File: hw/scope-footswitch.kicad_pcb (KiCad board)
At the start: 2 copper layers, 80 x 50 mm, 31 parts, among them J1 CN00050, J2 CN00023, J3 CN00049, SW1 M00027, SW2 M00012, SW3 M00026, Y1 Y00015

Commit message: Initial completion of schematic and layout
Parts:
- added C10: C00004, footprints:C_0805_2012M, F.Cu at (165.1, 82.5)
- added C11: C00033, footprints:C_0402_1005M, F.Cu at (143.8, 96.7)
- added C12: C00007, footprints:C_0603_1608M, F.Cu at (158.4, 100.5)
- added C13: C00001, footprints:C_0402_1005M, F.Cu at (158.6, 99.2)
- added C14: C00001, footprints:C_0402_1005M, F.Cu at (154.1, 89.0)
- added C15: C00001, footprints:C_0402_1005M, F.Cu at (151.6, 90.0)
- added C16: C00001, footprints:C_0402_1005M, F.Cu at (162.3, 90.7)
- added C17: C00001, footprints:C_0402_1005M, F.Cu at (160.4, 99.8)
- added C18: C00001, footprints:C_0402_1005M, F.Cu at (150.6, 95.2)
- added C19: C00001, footprints:C_0402_1005M, F.Cu at (128.6, 104.5)
- added C20: C00002, footprints:C_0603_1608M, F.Cu at (163.6, 90.5)
- added C21: C00001, footprints:C_0402_1005M, F.Cu at (128.6, 99.0)
- added C22: C00001, footprints:C_0402_1005M, F.Cu at (114.8, 86.5)
- added C23: C00001, footprints:C_0402_1005M, F.Cu at (165.6, 88.7)
- added C24: C00003, footprints:CRADIAL_6.3x11.2_2.5, F.Cu at (169.6, 106.7)
- added C25: C00027, footprints:C_0402_1005M, F.Cu at (182.2, 85.0)
- added C26: C00027, footprints:C_0402_1005M, F.Cu at (172.8, 112.8)
- added C27: C00001, footprints:C_0402_1005M, F.Cu at (168.2, 100.5)
- added C28: C00002, footprints:C_0603_1608M, F.Cu at (183.3, 95.0)
- added C29: C00001, footprints:C_0402_1005M, F.Cu at (179.4, 86.2)
- added D1: D00005, footprints:SOT_3_950_2900X1300X1000_ONSEMI, F.Cu at (175.6, 85.2)
- added P1: CN00052, footprints:P_FCI_68000-206, F.Cu at (148.4, 109.2)
- added P2: CN00051, footprints:P_CNC_3221-10-0300-00, F.Cu at (153.8, 79.7)
- added Q1: Q00002, footprints:SOT_6_650_2150X1300x1100_DIODES, F.Cu at (119.6, 86.5)
- added R12: R00038, footprints:R_0402_1005M, F.Cu at (134.8, 85.5)
- added R13: R00014, footprints:R_0402_1005M, F.Cu at (176.6, 92.2)
- added R14: R00009, footprints:R_0402_1005M, F.Cu at (176.6, 93.2)
- added R15: R00014, footprints:R_0402_1005M, F.Cu at (134.8, 97.0)
- added R16: R00014, footprints:R_0402_1005M, F.Cu at (133.6, 97.0)
- added R17: R00014, footprints:R_0402_1005M, F.Cu at (132.3, 97.0)
- added R18: R00014, footprints:R_0402_1005M, F.Cu at (148.8, 89.5)
- added R19: R00011, footprints:R_0402_1005M, F.Cu at (120.1, 102.7)
- added R20: R00011, footprints:R_0402_1005M, F.Cu at (120.1, 100.7)
- added R21: R00014, footprints:R_0402_1005M, F.Cu at (158.6, 101.8)
- added R22: R00014, footprints:R_0402_1005M, F.Cu at (127.1, 104.5)
- added R23: R00014, footprints:R_0402_1005M, F.Cu at (127.1, 99.0)
- added R24: R00014, footprints:R_0402_1005M, F.Cu at (127.8, 102.7)
- added R25: R00014, footprints:R_0402_1005M, F.Cu at (127.8, 100.7)
- added R26: R00014, footprints:R_0402_1005M, F.Cu at (114.1, 88.5)
- added R27: R00014, footprints:R_0402_1005M, F.Cu at (124.1, 87.0)
- added R28: R00014, footprints:R_0402_1005M, F.Cu at (113.3, 86.5)
- added R29: R00079, footprints:R_0603_1608M, F.Cu at (120.8, 89.0)
- added R30: R00014, footprints:R_0402_1005M, F.Cu at (122.6, 87.0)
- added R31: R00079, footprints:R_0603_1608M, F.Cu at (117.6, 89.0)
- added R32: R00014, footprints:R_0402_1005M, F.Cu at (163.1, 102.7)
- added R33: R00014, footprints:R_0402_1005M, F.Cu at (161.6, 99.8)
- added R34: R00047, footprints:R_0402_1005M, F.Cu at (170.6, 88.7)
- added R35: R00016, footprints:R_0402_1005M, F.Cu at (163.1, 109.5)
- added R36: R00047, footprints:R_0402_1005M, F.Cu at (168.1, 88.7)
- added R37: R00047, footprints:R_0402_1005M, F.Cu at (169.3, 88.7)
- added R38: R00047, footprints:R_0402_1005M, F.Cu at (166.8, 88.7)
- added R39: R00008, footprints:R_0402_1005M, F.Cu at (182.2, 83.8)
- added R40: R00008, footprints:R_0402_1005M, F.Cu at (172.8, 111.7)
- added R41: R00014, footprints:R_0402_1005M, F.Cu at (172.8, 85.2)
- added U1: U00054, footprints:SOT_5_950_2900X1600X1100_DIODES, F.Cu at (128.8, 86.5)
- added U2: U00086, footprints:SOT_6_950_2800x1600x110_DIODES_SOT26, F.Cu at (180.1, 93.2)
- added U3: U00055, footprints:SOIC_8_1270_4900X3900X1750, F.Cu at (134.3, 91.2)
- added U4: U00087, footprints:SOT_5_950_2900X1600X1100_DIODES, F.Cu at (148.1, 87.2)
- added U5: U00049, footprints:SOT_5_950_2900X1600X1100_DIODES, F.Cu at (165.1, 79.2)
- added U6: U00084, footprints:QFN_48_500_7000X7000X600_ST, F.Cu at (156.8, 93.7)
- added U7: U00085, footprints:MSOP_10_500_3000X3000X1100_ONSEMI, F.Cu at (168.8, 92.7)
- added U8: U00086, footprints:SOT_6_950_2800x1600x110_DIODES_SOT26, F.Cu at (163.6, 106.7)
- C2, C3: value C00033 -> C00001
- C5, C8: value C00002 -> C00001; footprint footprints:C_0603_1608M -> footprints:C_0402_1005M
- C6: value C00004 -> C00002; footprint footprints:C_0805_2012M -> footprints:C_0603_1608M
- C9: value C00001 -> C00033
- J2: value CN00023 -> CN00049; footprint footprints:J_FCI_10118194 -> footprints:J_AMPHENOL_UE27AC54100
- J3: value CN00049 -> CN00023; footprint footprints:J_AMPHENOL_UE27AC54100 -> footprints:J_FCI_10118194
- R10: value R00014 -> R00038
- R11, R4: value R00016 -> R00014
- R2: value R00025 -> R00016; footprint R_0603_1608M -> footprints:R_0402_1005M
- R7: value R00014 -> R00056
- R9: value R00009 -> R00037
- moved D5 79.6 mm to (180.1, 88.7), turned to 180 degrees
- moved J2 75.1 mm to (178.1, 104.7)
- moved SW1 57.4 mm to (186.0, 78.5)
- moved J1 57.3 mm to (110.6, 108.2)
- moved SW3 57.3 mm to (111.2, 94.2)
- moved D2 57.0 mm to (124.6, 80.2)
- moved SW2 57.0 mm to (139.6, 80.2)
- moved R7 54.5 mm to (172.2, 82.7), turned to 180 degrees
- moved D4 48.1 mm to (170.8, 99.5), turned to 270 degrees
- moved R3 44.9 mm to (155.7, 84.7), turned to 180 degrees
- moved Y1 41.7 mm to (146.8, 95.2), turned to 270 degrees
- moved J3 40.8 mm to (187.2, 88.2)
- moved R6 37.9 mm to (172.2, 81.6)
- moved R4 36.9 mm to (151.1, 84.7)
- moved C6 36.4 mm to (165.3, 76.2)
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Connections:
- C2 pad 1: GND -> /BTN
- C2 pad 2: Net-(C2-Pad2) -> GND
- C3 pad 1: GND -> +5V
- C3 pad 2: Net-(C3-Pad2) -> GND
- C4 pad 1: /BTN -> +5V
- C5 pad 1: GND -> +3V3
- C5 pad 2: +5V -> GND
- C6 pad 1: +3V3 -> GND
- C6 pad 2: GND -> +5V
- C7 pad 1: /HOST_VBUS -> +3V3
- C8 pad 1: GND -> +3V3
- C8 pad 2: VBUS -> GND
- C9 pad 1: VBUS -> GND
- C9 pad 2: GND -> Net-(C9-Pad2)
- D2 pad 2: Net-(D2-Pad2) -> GND
- D2 pad 3: (no net) -> /LED_DATA
- D2 pad 4: Net-(D2-Pad4) -> +5V
- D3 pad 1: Net-(D3-Pad1) -> /FOOTSW_BTN1_R
- D3 pad 2: Net-(D3-Pad2) -> GND
- D3 pad 3: Net-(D3-Pad3) -> /FOOTSW_BTN2_R
- D3 pad 4: Net-(D3-Pad4) -> /FOOTSW_BTN2_R
- D3 pad 5: Net-(D3-Pad5) -> +3V3
- D3 pad 6: Net-(D3-Pad6) -> /FOOTSW_BTN1_R
- D4 pad 1: Net-(D4-Pad1) -> /HOST_DP
- D4 pad 3: GND -> /HOST_DM
- D4 pad 4: GND -> /HOST_DM
- D4 pad 5: VBUS -> /HOST_VBUS
- D4 pad 6: Net-(D4-Pad6) -> /HOST_DP
- D5 pad 1: Net-(D5-Pad1) -> /DEVICE_DM
- D5 pad 3: Net-(D5-Pad3) -> /DEVICE_DP
- D5 pad 4: Net-(D5-Pad4) -> /DEVICE_DP
- D5 pad 5: /HOST_VBUS -> VBUS
- D5 pad 6: Net-(D5-Pad6) -> /DEVICE_DM
- J1 pad 1: Net-(J1-Pad1) -> GND
- J2 pad 1: VBUS -> /HOST_VBUS
- J2 pad 2: Net-(D4-Pad1) -> /HOST_DM
- J2 pad 3: Net-(D4-Pad6) -> /HOST_DP
- J2 pad 4: Net-(J2-Pad4) -> GND
- J2 pad M1: Net-(J2-PadM1) -> /HOST_SHIELD
- J2 pad M2: Net-(J2-PadM1) -> /HOST_SHIELD
- J3 pad 1: /HOST_VBUS -> VBUS
- J3 pad 2: Net-(D5-Pad1) -> /DEVICE_DM
- J3 pad 3: Net-(D5-Pad6) -> /DEVICE_DP
- J3 pad 4: GND -> Net-(J3-Pad4)
- J3 pad M1: Net-(J3-PadM1) -> /DEVICE_SHIELD
- J3 pad M2: Net-(J3-PadM2) -> /DEVICE_SHIELD
- R1 pad 1: /EN_DEVICE -> +3V3
- R1 pad 2: /EN_DEVICE_5V -> /UART_RX
- R10 pad 1: +3V3 -> /I2C_SDA
- R10 pad 2: /HOST_FAULT_N -> +3V3
- R11 pad 1: /HOST_ILIM -> GND
- R11 pad 2: GND -> Net-(R11-Pad2)
- R2 pad 1: /EN_DEVICE -> +3V3
- R2 pad 2: GND -> /SWDIO
- R3 pad 1: +3V3 -> /SWDCLK
- R3 pad 2: /SWDIO -> GND
- R4 pad 1: /SWDCLK -> +3V3
- R4 pad 2: GND -> /NRST
- R5 pad 1: /NRST -> /BTN_R
- R5 pad 2: +3V3 -> GND
- R6 pad 1: /BTN_R -> /EN_DEVICE
- R6 pad 2: /BTN -> /EN_DEVICE_5V
- R7 pad 1: /BTN -> GND
- R7 pad 2: GND -> /EN_DEVICE
- R8 pad 1: VBUS -> /BTN_R
- R8 pad 2: /VIN_FAULT_N -> /BTN
- R9 pad 1: /VIN_ILIM -> /LED_DATA
- R9 pad 2: GND -> /LED_DATA_R
- SW3 pad 2: Net-(SW3-Pad2) -> +3V3
- SW3 pad 3: Net-(SW3-Pad3) -> /MODE_R
- SW3 pad 5: Net-(SW3-Pad5) -> +3V3
- Y1 pad 1: Net-(C2-Pad2) -> Net-(C9-Pad2)
- Y1 pad 2: Net-(C3-Pad2) -> Net-(C11-Pad2)
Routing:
- net +3V3: track 0.00 -> 171.1 mm, vias 0 -> 10
- net +5V: track 0.00 -> 127.2 mm, vias 0 -> 4
- net GND: track 0.00 -> 100.7 mm, vias 0 -> 61
- net /MODE_LED_R: track 0.00 -> 53.1 mm, vias 0 -> 2
- net /MODE: track 0.00 -> 47.3 mm, vias 0 -> 2
- net /MODE_LED_G: track 0.00 -> 46.7 mm, vias 0 -> 2
- net /EN_DEVICE: track 0.00 -> 42.9 mm, vias 0 -> 4
- net /LED_DATA_LS: track 0.00 -> 33.1 mm, vias 0 -> 2
- net /FOOTSW_BTN2: track 0.00 -> 32.9 mm
- net /I2C_SCL: track 0.00 -> 32.6 mm, vias 0 -> 2
- net /FOOTSW_BTN1: track 0.00 -> 32.2 mm
- net VBUS: track 0.00 -> 29.9 mm, vias 0 -> 5
- net /I2C_SDA: track 0.00 -> 29.3 mm, vias 0 -> 2
- net /HOST_DM: track 0.00 -> 27.9 mm
- net /HOST_DP: track 0.00 -> 26.9 mm
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- added copper zone on B.Cu, net /DEVICE_SHIELD
- added copper zone on F.Cu, net /DEVICE_SHIELD
- added copper zone on B.Cu, net /HOST_SHIELD
- added copper zone on F.Cu, net /HOST_SHIELD
- added copper zone on B.Cu, net GND
- added copper zone on F.Cu, net GND
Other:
- net class Default: clearance 0.2 -> 0.16; trace_width 0.25 -> 0.16; via_dia 0.8 -> 0.6; via_drill 0.4 -> 0.26
- net class POWER added: clearance 0.16, trace_width 0.3, via_dia 0.6, via_drill 0.26
- net class USB added: clearance 0.16, trace_width 0.3, via_dia 0.6, via_drill 0.26
- rule pad_to_mask_clearance: 0.2 -> 0.0508
- rule trace_clearance: 0.2 -> 0.16
- rule trace_min: 0.2 -> 0.16
- rule via_min_drill: 0.3 -> 0.26
- rule via_min_size: 0.4 -> 0.6
- board text added: "scope-footswitch R1.0 2018-08-10 Paul Roukema"

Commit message: PCB updates and output files
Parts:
- moved J1 1.30 mm to (109.3, 108.2)
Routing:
- net Net-(J1-Pad3): track 4.48 -> 5.41 mm
- net Net-(J1-Pad2): track 9.71 -> 10.2 mm
- net GND: vias 61 -> 93
- net (no net): vias 0 -> 32

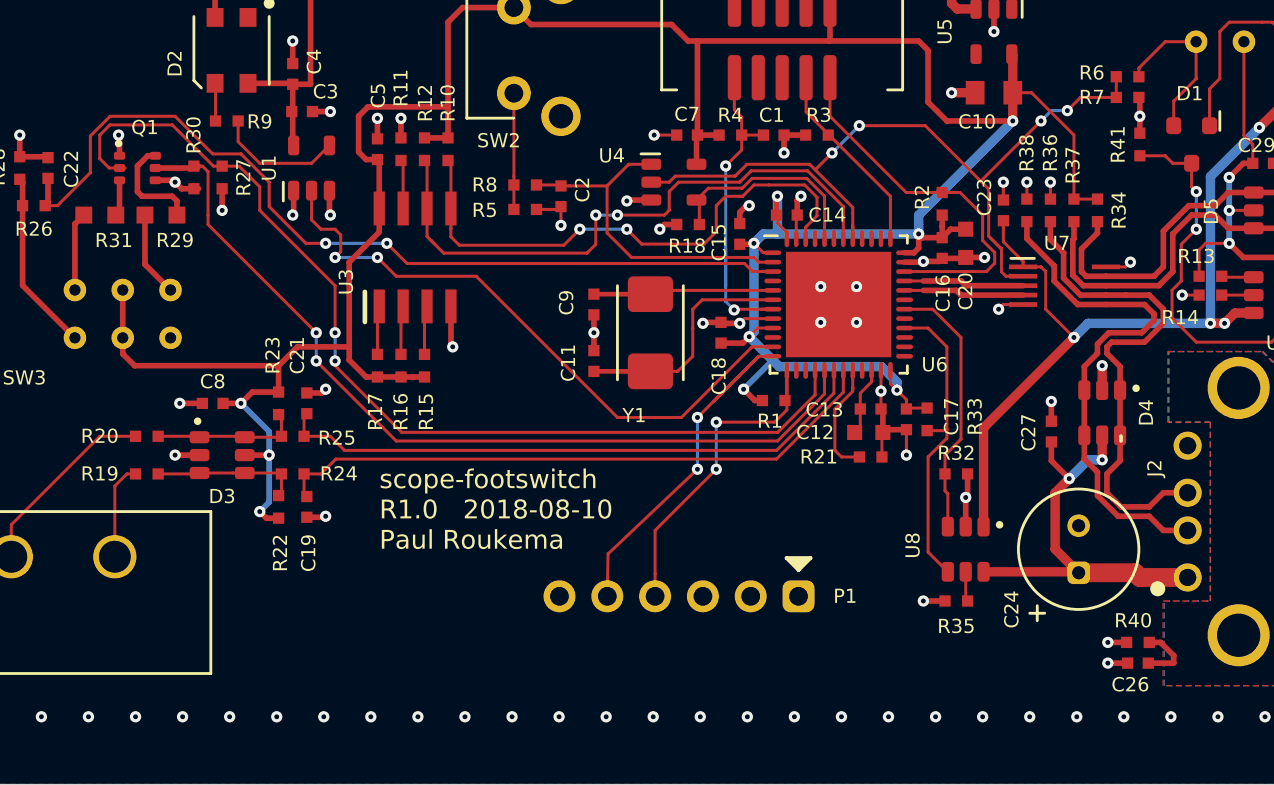
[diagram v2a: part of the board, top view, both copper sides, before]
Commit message: Layout V1.1 Fix unconnected vias, pour under crystal, USB switch pads
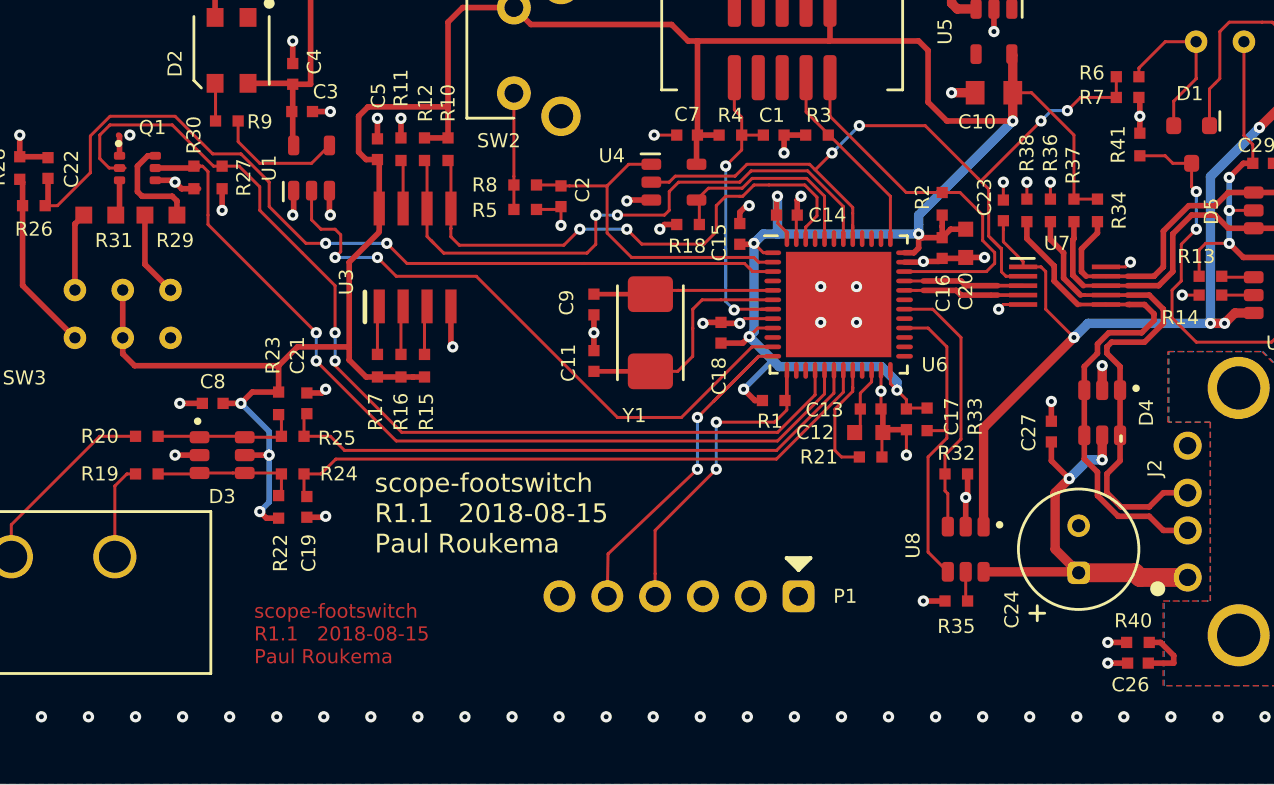
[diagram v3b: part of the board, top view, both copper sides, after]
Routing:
- net GND: vias 93 -> 125
- net (no net): vias 32 -> 0
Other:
- board text added: "scope-footswitch R1.1 2018-08-15 Paul Roukema"
- board text removed: "scope-footswitch R1.0 2018-08-10 Paul Roukema"

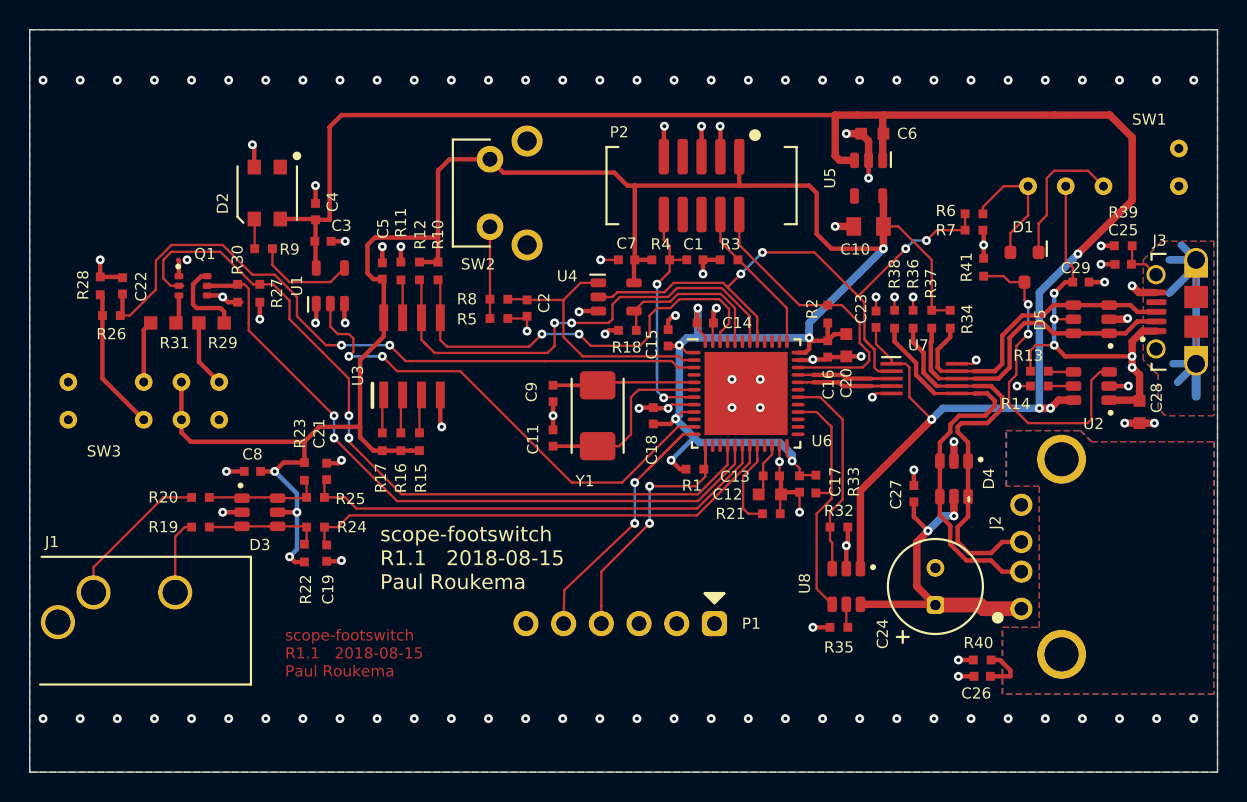
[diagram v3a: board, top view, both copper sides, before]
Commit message: HW Rev 13
Tweak/DNP a bunch of parts to allow simplified power/boot control
Update layout, including mechanical tweaks for better panel layout
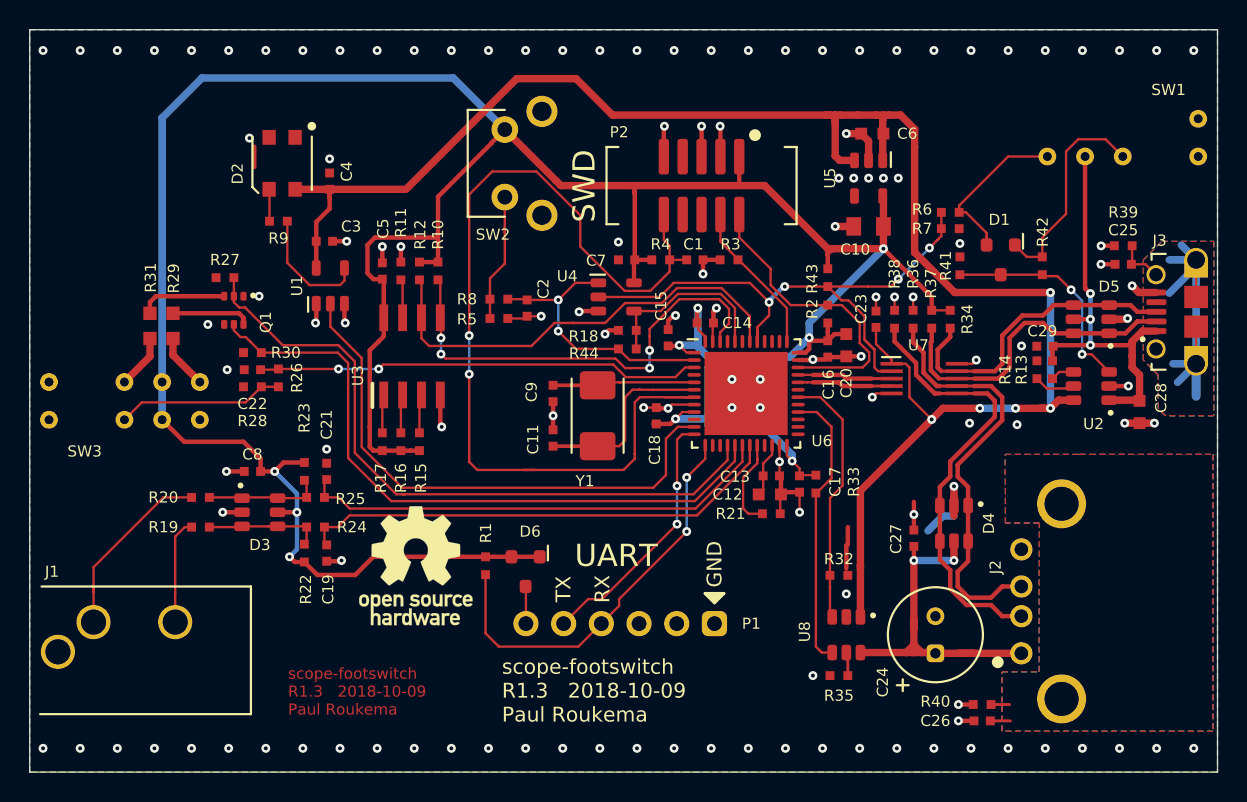
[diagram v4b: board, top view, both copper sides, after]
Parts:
- added D6: D00006, footprints:SOT_3_950_2900X1300X1000_ONSEMI, F.Cu at (142.0, 105.7)
- added M1: M00028, footprints:OSHW-Logo_7.5x8mm_SilkScreen, F.Cu at (134.6, 105.3)
- added R42: R00001, footprints:R_0402_1005M, F.Cu at (176.8, 85.1)
- added R43: R00046, footprints:R_0402_1005M, F.Cu at (162.3, 85.9)
- added R44: R00001, footprints:R_0402_1005M, F.Cu at (148.8, 90.7)
- D1: value D00005 -> D00006
- R29, R31: value R00079 -> R00080
- R34, R37: value R00047 -> R00081
- R36, R38: value R00047 -> R00056
- moved R1 15.5 mm to (139.3, 105.3), turned to 270 degrees
- moved R28 12.3 mm to (123.6, 93.2), turned to 180 degrees
- moved R26 12.0 mm to (125.3, 92.7), turned to 90 degrees
- moved C22 10.4 mm to (123.6, 92.1), turned to 180 degrees
- moved C29 4.95 mm to (177.0, 90.5), turned to 180 degrees
- moved R30 4.12 mm to (123.6, 91.0), turned to 180 degrees
- moved C24 3.25 mm to (169.6, 110.0)
- moved R32 3.25 mm to (163.1, 106.0)
- moved R35 3.25 mm to (163.1, 112.7)
- moved U8 3.25 mm to (163.6, 110.0)
- moved Q1 3.21 mm to (122.3, 88.1), turned to 270 degrees
- moved C26 3.00 mm to (172.8, 115.8)
- moved C27 3.00 mm to (168.2, 103.5)
- moved D4 3.00 mm to (170.8, 102.5)
- moved J2 3.00 mm to (178.1, 107.7)
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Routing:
- net +3V3: track 171.1 -> 234.7 mm, vias 10 -> 9
- net /NRST: track 19.0 -> 65.6 mm
- net /MODE: track 47.3 -> 30.0 mm
- net GND: track 100.7 -> 87.8 mm, vias 125 -> 129
- net /UART_RX: track 18.4 -> 27.7 mm
- net /MODE_LED_R: track 53.1 -> 45.9 mm, vias 2 -> 0
- net /PWR_EN: track 22.0 -> 14.8 mm
- net +5V: track 127.2 -> 121.0 mm, vias 4 -> 5
- net /EN_HOST_5V: track 9.69 -> 14.7 mm
- net /LED_DATA_LS: track 33.1 -> 37.2 mm, vias 2 -> 0
- net Net-(Q1-Pad3): track 1.93 -> 5.92 mm
- net /BTN_R: track 6.18 -> 9.42 mm
- net /HOST_VBUS_EN: track 14.1 -> 17.2 mm
- net /UART_TX: track 20.3 -> 17.4 mm
- net /HOST_FAULT_N: track 16.5 -> 19.2 mm
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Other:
- board text added: "GND"
- board text added: "RX"
- board text added: "SWD"
- board text added: "TX"
- board text added: "UART"
- board text added: "scope-footswitch R1.3 2018-10-09 Paul Roukema"
- board text removed: "scope-footswitch R1.1 2018-08-15 Paul Roukema"

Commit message: Rev 1.4, increase via hole size to 0.3mm
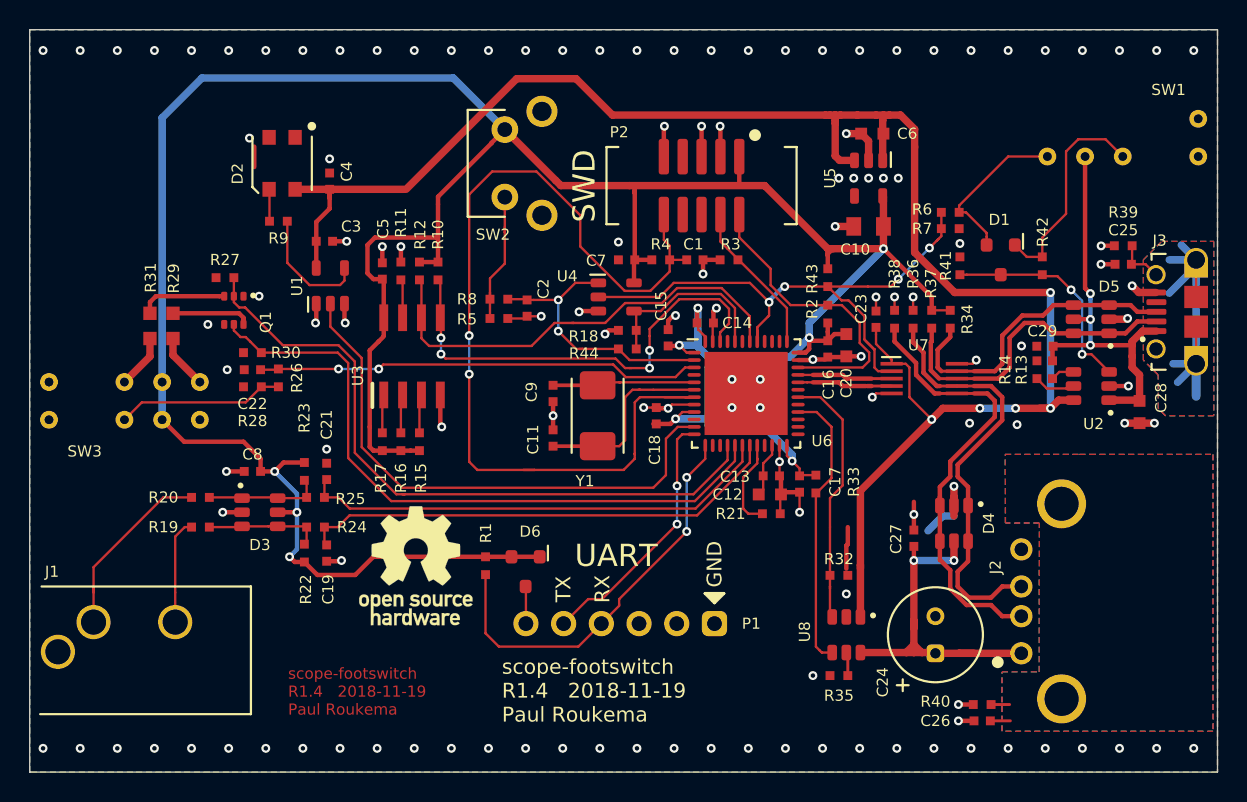
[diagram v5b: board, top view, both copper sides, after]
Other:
- net class Default: via_drill 0.26 -> 0.3
- net class POWER: via_drill 0.26 -> 0.3
- net class USB: via_drill 0.26 -> 0.3
- rule via_min_drill: 0.26 -> 0.3
- board text added: "scope-footswitch R1.4 2018-11-19 Paul Roukema"
- board text removed: "scope-footswitch R1.3 2018-10-09 Paul Roukema"
